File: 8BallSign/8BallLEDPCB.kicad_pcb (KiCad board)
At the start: 2 copper layers, 27.9 x 76.2 mm, 0 parts

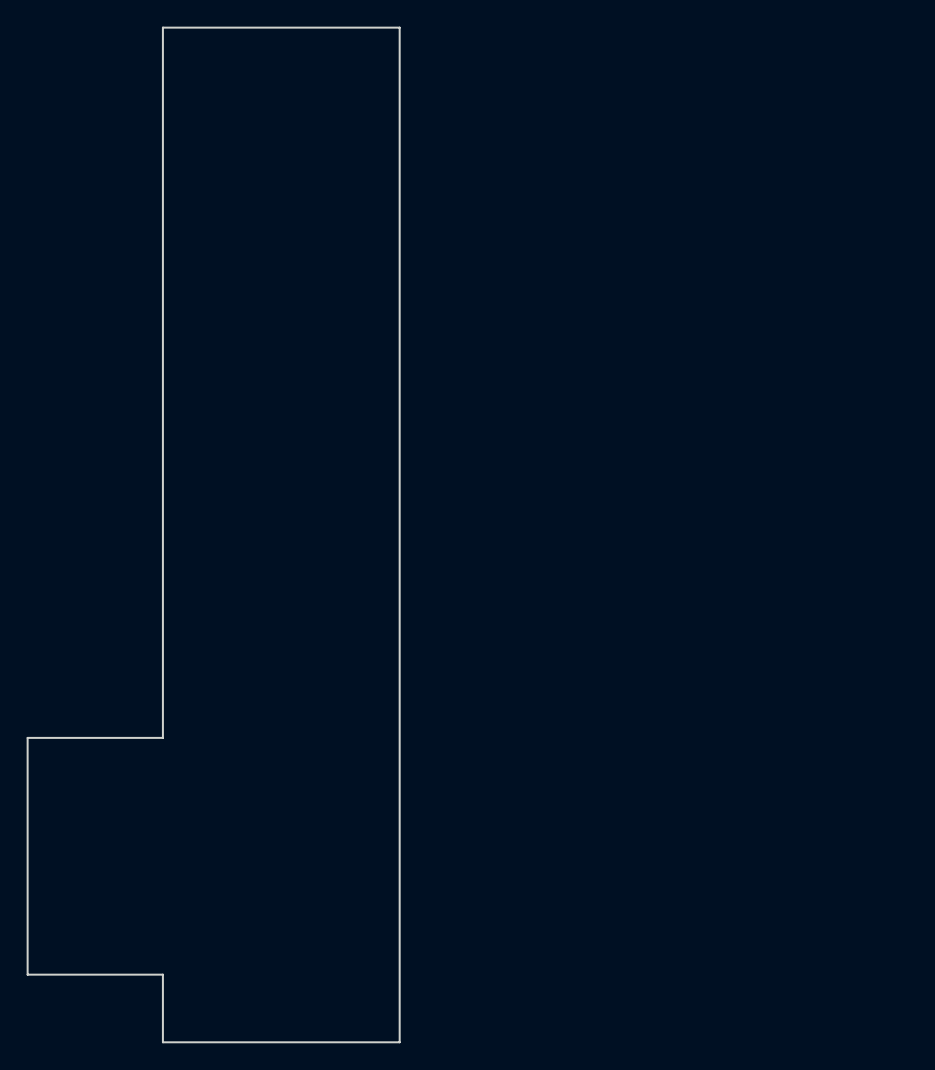
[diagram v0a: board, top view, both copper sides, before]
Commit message: Completed 8-ball club sign.
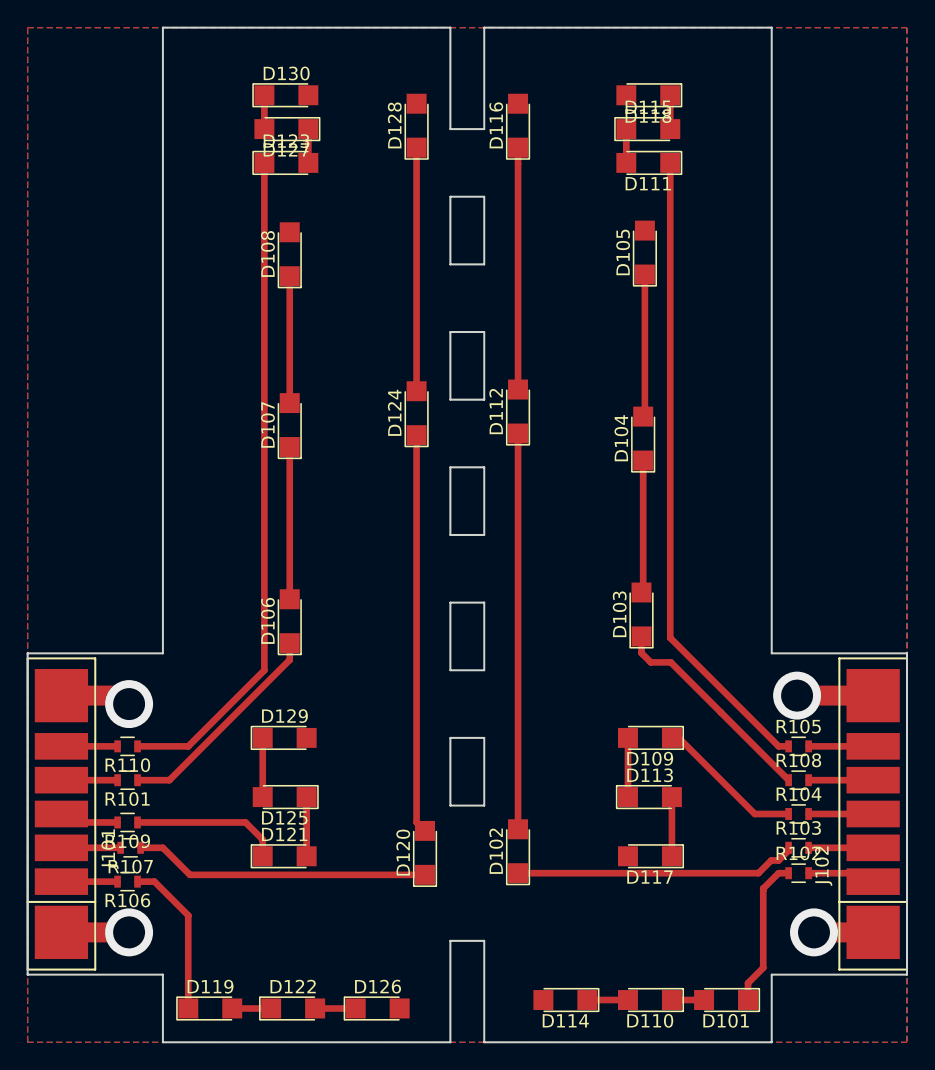
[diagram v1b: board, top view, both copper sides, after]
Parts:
- added D101: ARROW, LEDs:LED_1206, F.Cu at (105.8, 113.7)
- added D102: CUE, LEDs:LED_1206, F.Cu at (90.2, 102.5)
- added D103: BALL, LEDs:LED_1206, F.Cu at (99.4, 84.7)
- added D104: BALL, LEDs:LED_1206, F.Cu at (99.6, 71.5)
- added D105: BALL, LEDs:LED_1206, F.Cu at (99.7, 57.5)
- added D106: BALL, LEDs:LED_1206, F.Cu at (73.0, 85.2)
- added D107: BALL, LEDs:LED_1206, F.Cu at (73.0, 70.5)
- added D108: BALL, LEDs:LED_1206, F.Cu at (73.0, 57.7)
- added D109: CLUB, LEDs:LED_1206, F.Cu at (100.1, 94.0)
- added D110: ARROW, LEDs:LED_1206, F.Cu at (100.1, 113.7)
- added D111: 8BALL, LEDs:LED_1206, F.Cu at (100.0, 50.8)
- added D112: CUE, LEDs:LED_1206, F.Cu at (90.2, 69.5)
- added D113: CLUB, LEDs:LED_1206, F.Cu at (100.1, 98.4)
- added D114: ARROW, LEDs:LED_1206, F.Cu at (93.7, 113.7)
- added D115: 8BALL, LEDs:LED_1206, F.Cu at (100.0, 48.3)
- added D116: CUE, LEDs:LED_1206, F.Cu at (90.2, 48.0)
- added D117: CLUB, LEDs:LED_1206, F.Cu at (100.1, 102.9)
- added D118: 8BALL, LEDs:LED_1206, F.Cu at (100.0, 45.7)
- added D119: ARROW, LEDs:LED_1206, F.Cu at (67.1, 114.3)
- added D120: CUE, LEDs:LED_1206, F.Cu at (83.2, 102.6)
- added D121: CLUB, LEDs:LED_1206, F.Cu at (72.6, 102.9)
- added D122: ARROW, LEDs:LED_1206, F.Cu at (73.3, 114.3)
- added D123: 8BALL, LEDs:LED_1206, F.Cu at (72.8, 50.8)
- added D124: CUE, LEDs:LED_1206, F.Cu at (82.5, 69.6)
- added D125: CLUB, LEDs:LED_1206, F.Cu at (72.6, 98.4)
- added D126: ARROW, LEDs:LED_1206, F.Cu at (79.6, 114.3)
- added D127: 8BALL, LEDs:LED_1206, F.Cu at (72.8, 48.3)
- added D128: CUE, LEDs:LED_1206, F.Cu at (82.5, 48.0)
- added D129: CLUB, LEDs:LED_1206, F.Cu at (72.6, 94.0)
- added D130: 8BALL, LEDs:LED_1206, F.Cu at (72.8, 45.7)
- added J101: Solder pads, SolderPads:PowerPlus5, F.Cu at (55.9, 99.7)
- added J102: Solder pads, SolderPads:PowerPlus5, F.Cu at (116.8, 99.7)
- added R101: 150, Resistors_SMD:R_0603, F.Cu at (60.8, 97.2)
- added R102: 150, Resistors_SMD:R_0603, F.Cu at (111.2, 104.1)
- added R103: 150, Resistors_SMD:R_0603, F.Cu at (111.2, 102.2)
- added R104: 150, Resistors_SMD:R_0603, F.Cu at (111.2, 99.7)
- added R105: 150, Resistors_SMD:R_0603, F.Cu at (111.2, 94.6)
- added R106: 150, Resistors_SMD:R_0603, F.Cu at (60.8, 104.8)
- added R107: 150, Resistors_SMD:R_0603, F.Cu at (61.1, 102.2)
- added R108: 150, Resistors_SMD:R_0603, F.Cu at (111.2, 97.2)
- added R109: 150, Resistors_SMD:R_0603, F.Cu at (60.8, 100.3)
- added R110: 150, Resistors_SMD:R_0603, F.Cu at (60.8, 94.6)
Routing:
- net Net-(D123-Pad1): track 0.00 -> 50.0 mm
- net Net-(D111-Pad1): track 0.00 -> 47.9 mm
- net Net-(D120-Pad2): track 0.00 -> 30.0 mm
- net Net-(D102-Pad2): track 0.00 -> 29.7 mm
- net Net-(D120-Pad1): track 0.00 -> 22.2 mm
- net Net-(D102-Pad1): track 0.00 -> 21.2 mm
- net +VDC: track 0.00 -> 20.6 mm, vias 0 -> 4
- net Net-(D124-Pad2): track 0.00 -> 18.3 mm
- net Net-(D112-Pad2): track 0.00 -> 18.2 mm
- net Net-(D106-Pad1): track 0.00 -> 16.4 mm
- net Net-(D103-Pad1): track 0.00 -> 16.3 mm
- net Net-(D119-Pad1): track 0.00 -> 11.8 mm
- net Net-(D106-Pad2): track 0.00 -> 11.4 mm
- net Net-(D101-Pad1): track 0.00 -> 11.3 mm
- net Net-(D121-Pad1): track 0.00 -> 11.2 mm
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- added copper zone on B.Cu, net +VDC
- added copper zone on F.Cu, net +VDC
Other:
- board size 27.9 x 76.2 mm -> 66 x 76.2 mm

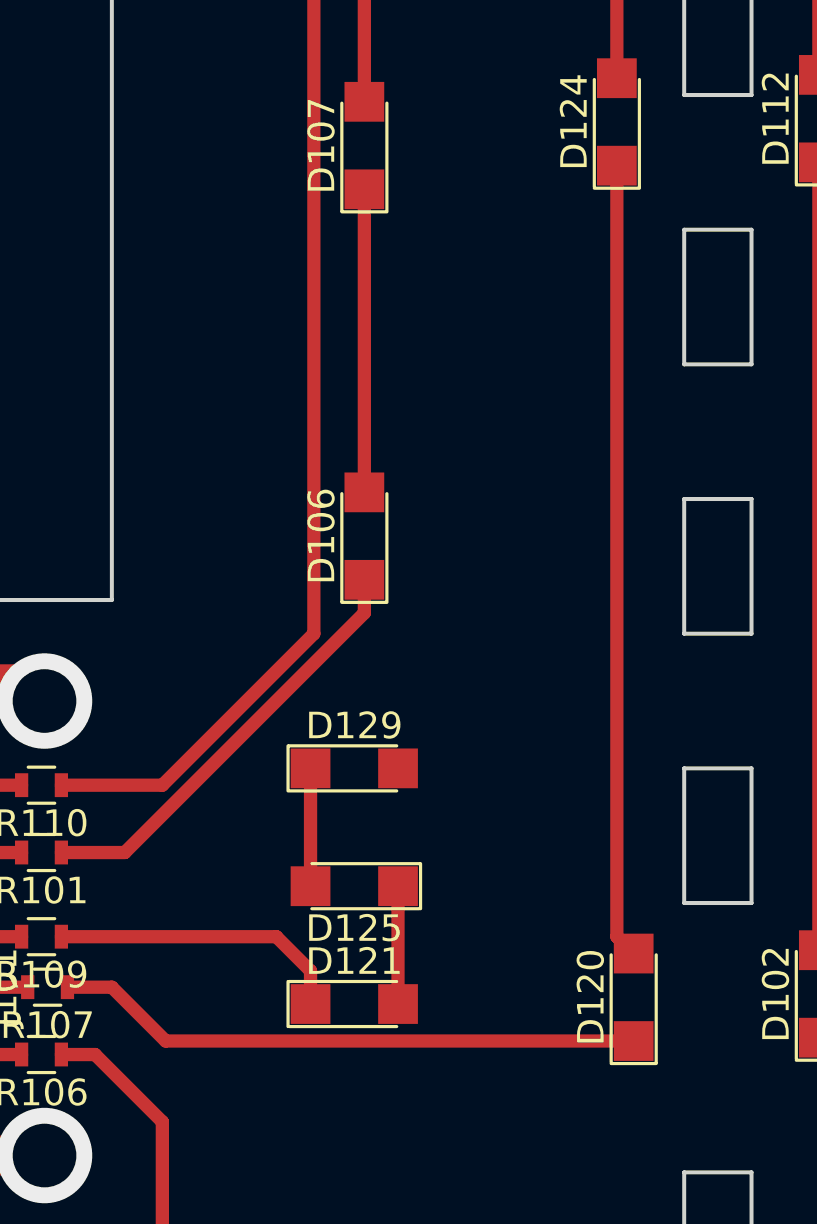
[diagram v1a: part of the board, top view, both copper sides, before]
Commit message: Final updates to 8 Ball Club sign.
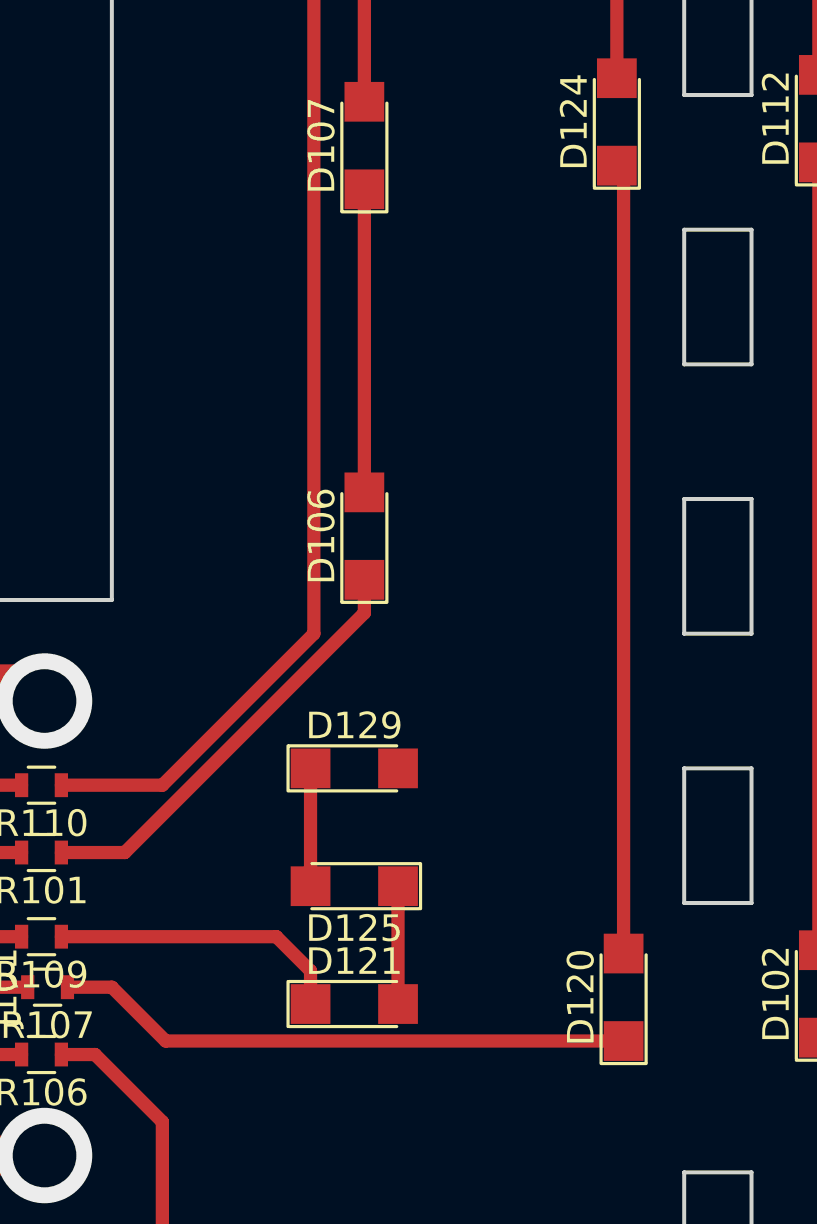
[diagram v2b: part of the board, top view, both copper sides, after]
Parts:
- moved D120 0.38 mm to (82.8, 102.6)
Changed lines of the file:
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@@
     (links 53)
     (no_connects 0)
-    (area 20.793469 15.08 137.39 130.335001)
+    (area 53.264999 40.564999 119.455001 116.915001)
     (thickness 1.6)
-    (drawings 60)
+    (drawings 65)
     (tracks 89)
     (zones 0)
@@
   )
   (setup
-    (last_trace_width 1.5)
+    (last_trace_width 0.5)
     (user_trace_width 0.5)
     (user_trace_width 1)
@@
   )
   (module LEDs:LED_1206 (layer F.Cu)
-    (at 83.185 102.615 90)
+    (at 82.804 102.615 90)
     (descr "LED 1206 smd package")
     (tags "LED led 1206 SMD smd SMT smt smdled SMDLED smtled SMTLED")
@@
     )
   )
+  (dimension 21.59 (width 0.3) (layer Dwgs.User)
+    (gr_text "21.590 mm" (at 74.295 123.524) (layer Dwgs.User)
+      (effects (font (size 1.5 1.5) (thickness 0.3)))
+    )
+    (feature1 (pts (xy 85.09 116.84) (xy 85.09 124.874)))
+    (feature2 (pts (xy 63.5 116.84) (xy 63.5 124.874)))
+    (crossbar (pts (xy 63.5 122.174) (xy 85.09 122.174)))
+    (arrow1a (pts (xy 85.09 122.174) (xy 83.963496 122.760421)))
+    (arrow1b (pts (xy 85.09 122.174) (xy 83.963496 121.587579)))
+    (arrow2a (pts (xy 63.5 122.174) (xy 64.626504 122.760421)))
+    (arrow2b (pts (xy 63.5 122.174) (xy 64.626504 121.587579)))
+  )
+  (gr_line (start 89.154 46.228) (end 89.154 122.936) (layer Dwgs.User) (width 0.2))
+  (gr_line (start 83.82 104.394) (end 83.82 36.83) (layer Dwgs.User) (width 0.2))
+  (gr_line (start 91.186 46.228) (end 91.186 119.634) (layer Dwgs.User) (width 0.2))
+  (gr_line (start 81.534 46.228) (end 81.534 122.682) (layer Dwgs.User) (width 0.2))
   (dimension 13.97 (width 0.3) (layer Dwgs.User)
     (gr_text "13.970 mm" (at 29.13 109.855 90) (layer Dwgs.User)
@@
   (segment (start 65.405 107.315) (end 62.865 104.775) (width 0.5) (layer F.Cu) (net 31))
   (segment (start 62.865 104.775) (end 61.595 104.775) (width 0.5) (layer F.Cu) (net 31))
-  (segment (start 82.55 71.245) (end 82.55 100.33) (width 0.5) (layer F.Cu) (net 32))
-  (segment (start 82.55 100.33) (end 83.185 100.965) (width 0.5) (layer F.Cu) (net 32))
+  (segment (start 82.804 100.965) (end 82.804 71.499) (width 0.5) (layer F.Cu) (net 32))
+  (segment (start 82.804 71.499) (end 82.55 71.245) (width 0.5) (layer F.Cu) (net 32))
+  (segment (start 65.53 104.265) (end 82.804 104.265) (width 0.5) (layer F.Cu) (net 33))
   (segment (start 63.5 102.235) (end 61.825 102.235) (width 0.5) (layer F.Cu) (net 33))
   (segment (start 65.53 104.265) (end 63.5 102.235) (width 0.5) (layer F.Cu) (net 33))
-  (segment (start 83.185 104.265) (end 65.53 104.265) (width 0.5) (layer F.Cu) (net 33))
   (segment (start 74.295 102.87) (end 74.295 98.425) (width 0.5) (layer F.Cu) (net 34))
   (segment (start 61.595 100.33) (end 69.705 100.33) (width 0.5) (layer F.Cu) (net 35))

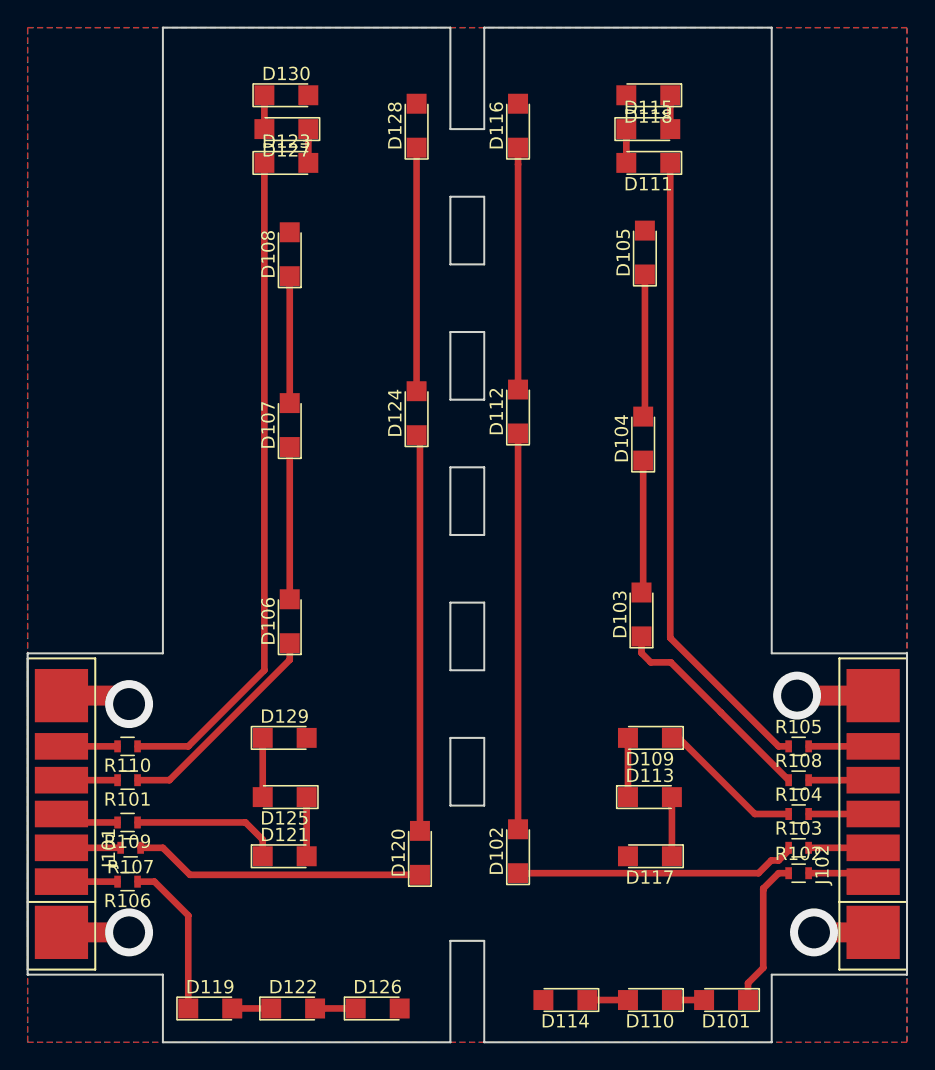
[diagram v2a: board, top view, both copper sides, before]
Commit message: Single PCB version (thinner sign).
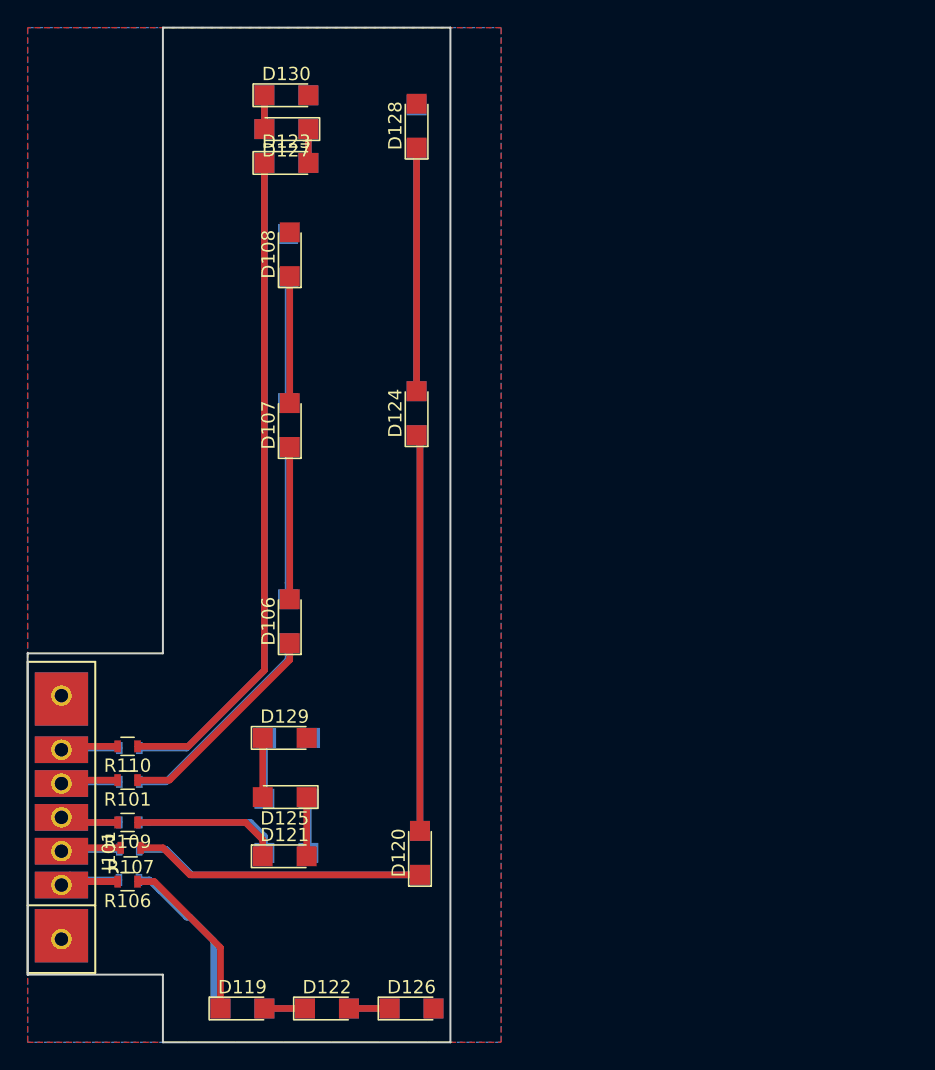
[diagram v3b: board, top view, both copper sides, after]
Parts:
- removed J102: Solder pads, SolderPads:PowerPlus5
- D101, D102, D103, D104, D105, D109, D110, D111, D112, D113, D114, D115, D116, D117, D118, R102, R103, R104, R105, R108: moved to B.Cu
- J101: footprint SolderPads:PowerPlus5 -> PowerPlus5X2
- moved R102 50.3 mm to (60.9, 104.6), turned to 180 degrees
- moved R104 50.3 mm to (61.0, 100.3), turned to 180 degrees
- moved R103 50.3 mm to (61.0, 102.4), turned to 180 degrees
- moved R105 50.3 mm to (61.0, 94.7), turned to 180 degrees
- moved R108 50.3 mm to (61.0, 97.3), turned to 180 degrees
- moved D101 36.3 mm to (69.5, 114.3), turned to 0 degrees
- moved D109 28.6 mm to (72.8, 102.6), turned to 0 degrees
- moved D117 28.6 mm to (72.9, 94.0), turned to 0 degrees
- moved D113 27.3 mm to (72.8, 98.6), turned to 180 degrees
- moved D115 27.2 mm to (72.8, 48.3), turned to 180 degrees
- moved D111 27.2 mm to (72.8, 50.8), turned to 0 degrees
- moved D118 27.2 mm to (72.8, 45.7), turned to 0 degrees
- moved D105 26.8 mm to (72.9, 57.8)
- moved D104 26.7 mm to (72.9, 70.5)
- moved D103 26.5 mm to (72.9, 85.2)
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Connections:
- J101 pad 2: /AL -> /A
- J101 pad 3: /BL -> /B
- J101 pad 4: /CL -> /C
- J101 pad 5: /DL -> /D
- J101 pad 6: /EL -> /E
- R101 pad 2: /DL -> /D
- R102 pad 2: /AR -> /A
- R103 pad 2: /BR -> /B
- R104 pad 2: /CR -> /C
- R105 pad 2: /ER -> /E
- R106 pad 2: /AL -> /A
- R107 pad 2: /BL -> /B
- R108 pad 2: /DR -> /D
- R109 pad 2: /CL -> /C
- R110 pad 2: /EL -> /E
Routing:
- net +VDC: track 20.6 -> 0.00 mm, vias 4 -> 0
- net /A: track 0.00 -> 13.9 mm
- net /E: track 0.00 -> 10.5 mm
- net /B: track 0.00 -> 9.74 mm
- net /C: track 0.00 -> 8.98 mm
- net /D: track 0.00 -> 8.61 mm
- net /AR: track 7.91 -> 0.00 mm
- net /EL: track 6.12 -> 0.00 mm
- net /CR: track 5.85 -> 0.00 mm
- net /BL: track 5.34 -> 0.00 mm
- net /AL: track 5.11 -> 0.00 mm
- net /ER: track 4.85 -> 0.00 mm
- net /DR: track 4.85 -> 0.00 mm
- net /BR: track 4.85 -> 0.00 mm
- net /CL: track 4.48 -> 0.00 mm
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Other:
- board size 66 x 76.2 mm -> 31.8 x 76.2 mm
